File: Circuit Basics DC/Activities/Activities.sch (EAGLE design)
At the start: 34 parts

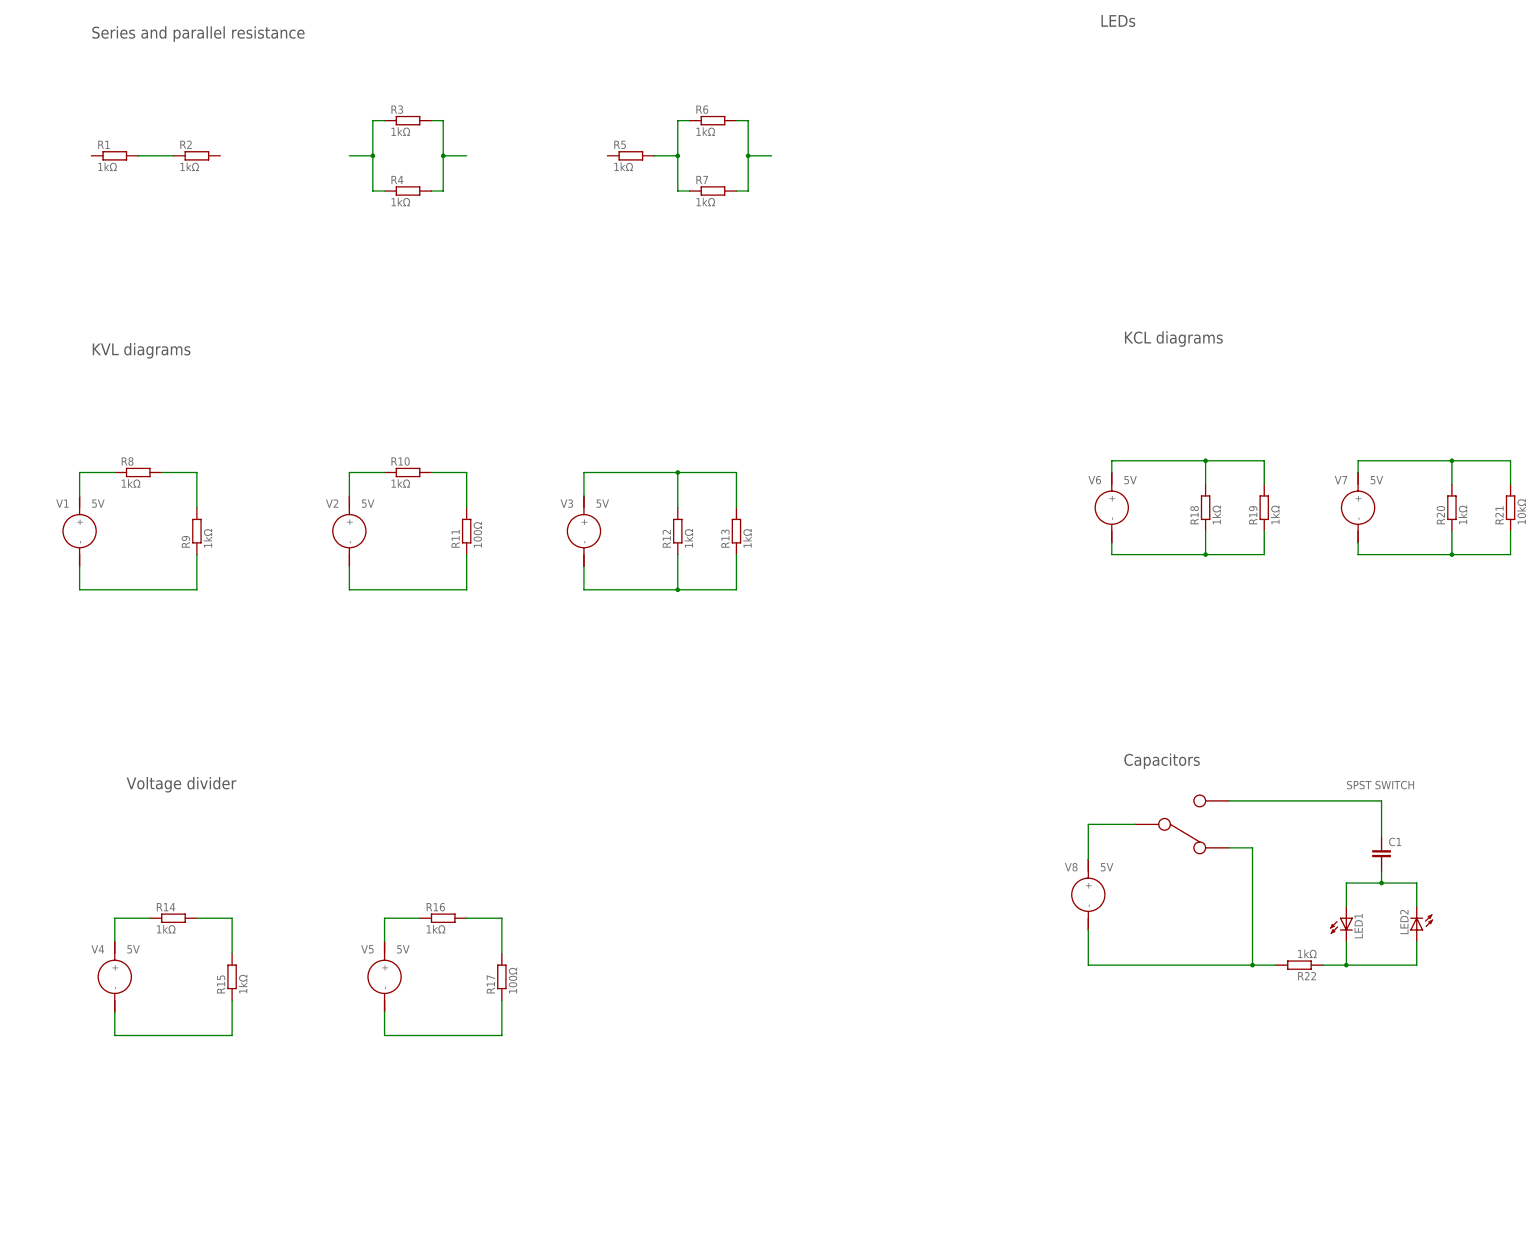
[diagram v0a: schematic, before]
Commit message: corrected schematics; updated readme
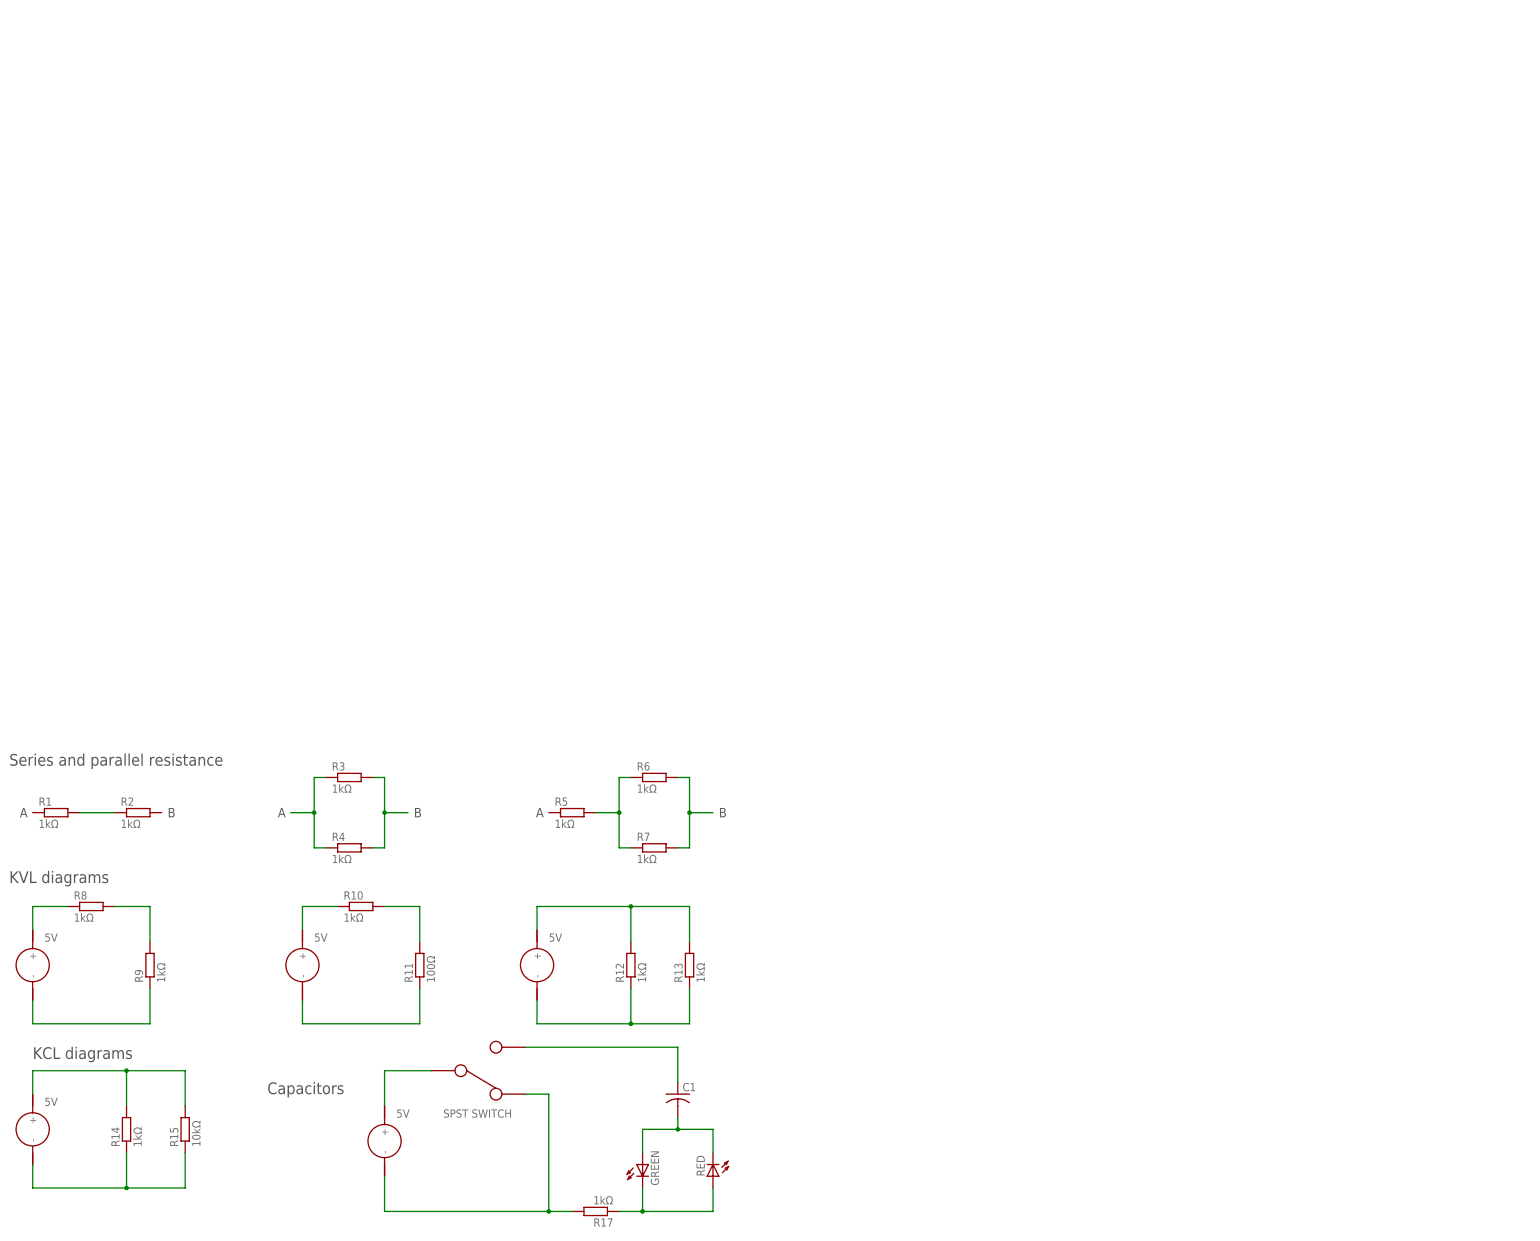
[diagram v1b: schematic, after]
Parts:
- removed LED1, LED2: (no value), led:LED3MM
- removed R16, R18, R19, R20, R22: 1kΩ, rcl:R-EU_0207/10
- removed R21: 10kΩ, rcl:R-EU_0207/10
- removed V4, V5, V6: 5V, personal:VOLTAGE_SOURCE
- added GREEN, RED: (no value), led:LED3MM
- C1: device rcl:C-EU025-025X050 -> rcl:C-US025-025X050
- R15: value 1kΩ -> 10kΩ
- R17: value 100Ω -> 1kΩ
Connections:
- removed net N$14: R14.1, V4.+
- removed net N$15: R14.2, R15.2
- removed net N$16: R15.1, V4.-
- removed net N$17: R17.1, V5.-
- removed net N$18: R16.2, R17.2
- removed net N$19: R16.1, V5.+
- removed net N$26: R18.2, R19.2, V6.+
- removed net N$27: R18.1, R19.1, V6.-
- net N$20: now also R17.2; no longer R22.2
- net N$23: now also GREEN.A, RED.C; no longer LED1.A, LED2.C
- net N$25: now also GREEN.C, R17.1, RED.A; no longer LED1.C, LED2.A, R22.1
- net N$28: now also R14.2, R15.2; no longer R20.2, R21.2
- net N$29: now also R14.1, R15.1; no longer R20.1, R21.1
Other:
- note added: "A"
- note added: "B"
- note removed: "LEDs"
- note removed: "Voltage divider"
- moved on the sheet: C1, R1, R10, R11, R12, R13, R14, R15, R17, R2, R3, R4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

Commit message: fixed diagrams
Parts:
- added R16, R18: 1kΩ, rcl:R-EU_0207/10
- added R19, R20: 10kΩ, rcl:R-EU_0207/10
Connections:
- new net N$14: R16.2, R18.2, R19.2, R20.2
- new net N$15: R16.1, R18.1, R19.1, R20.1
- net N$21: now also U$1.A; no longer U$1.IN
- net N$22: now also U$1.IN; no longer U$1.A
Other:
- note added: "SPDT SWITCH"
- note removed: "Capacitors"
- note removed: "SPST SWITCH"
- moved on the sheet: C1, GREEN, R1, R17, R2, R5, R6, R7, RED
